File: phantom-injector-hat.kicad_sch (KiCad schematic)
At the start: 40 parts, among them J1 Conn_02x20_Odd_Even, J2 Conn_02x03_Top_Bottom, J3 Conn_01x03, J4 Conn_01x03, SW1 SW_SPST, U1 LT8362EMSE-PBF

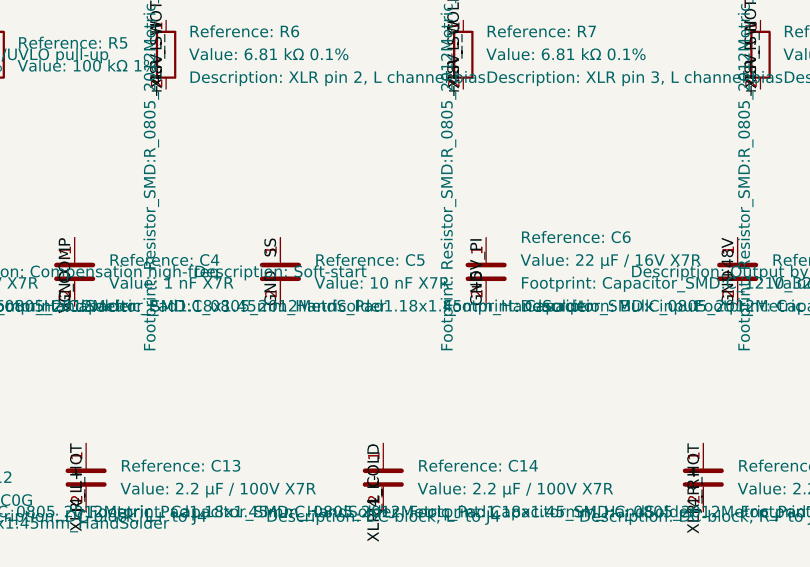
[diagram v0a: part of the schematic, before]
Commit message: Raise C5 soft-start cap from 10nF to 22nF; resolve item #7
Analytical Pi 5V inrush check (DESIGN_DOC §6 item 7) found the
original 10 nF gives a calculated ~750 mA input draw for 8 ms
during soft-start — over the 600 mA HAT continuous spec.

Bumping C5 to 22 nF lengthens t_ss from ~8 ms to ~17.6 ms,
cutting peak input current to ~342 mA (comfortably under HAT
budget). Steady-state input draw post-startup is ~34 mA at
full phantom load. Tradeoff is a 10 ms slower startup —
irrelevant for phantom power.

Schematic, BOM, DigiKey order CSV, and DESIGN_DOC all updated.
Sourced as Kemet 399-17886-1-ND after Yageo CC0805 Mfr PN
mis-resolved on DigiKey order pad.

Co-Authored-By: Claude Opus 4.7 <noreply@anthropic.com>
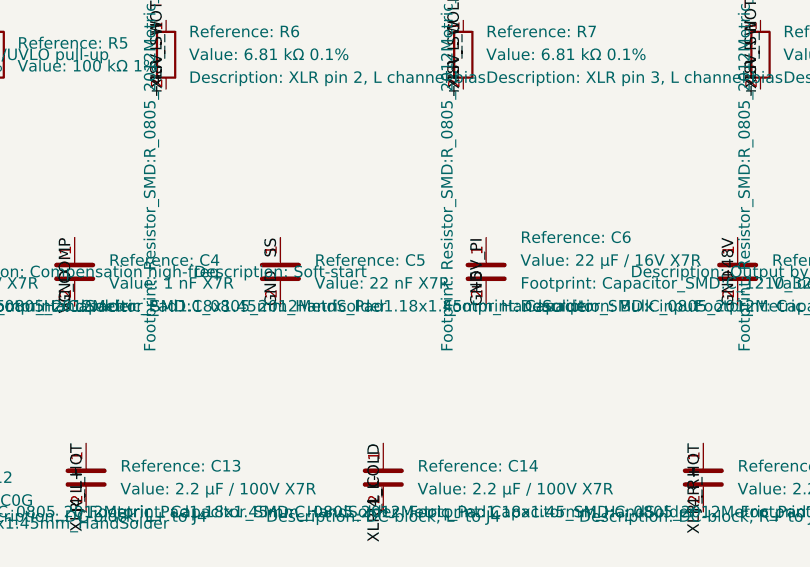
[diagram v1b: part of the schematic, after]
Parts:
- C5: value 10 nF X7R -> 22 nF X7R

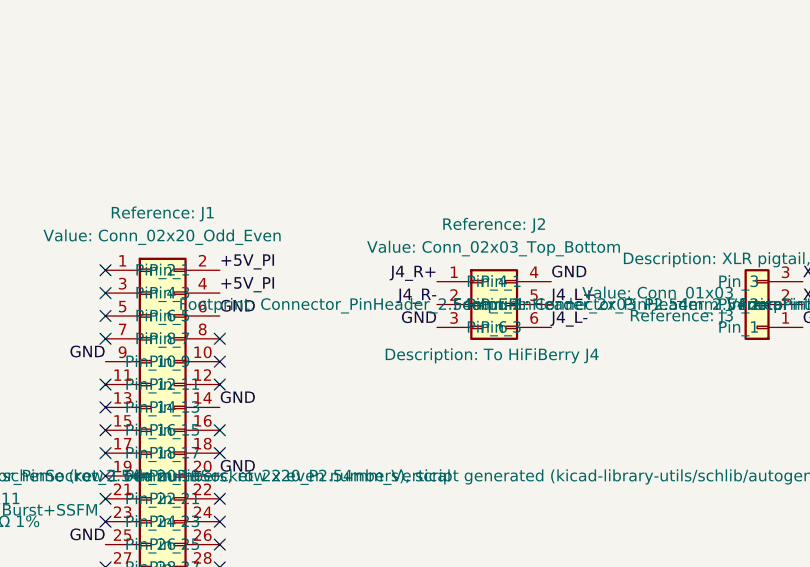
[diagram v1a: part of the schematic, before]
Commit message: Fix J2 right channel R+/R- swap; resolve item #5
Re-verified §3.4 HiFiBerry J4 pinout against the DAC2 ADC Pro
datasheet (hifiberry.com/docs/data-sheets/datasheet-dac2-adc-pro/).
Found a bug: §3.4 had J2 pin 1 = R+, pin 2 = R-, but the datasheet
specifies pin 1 = in R-, pin 2 = in R+ (pin 1 = left bottom corner).
Without the fix the right channel polarity would be inverted vs
the left, breaking stereo imaging and partially cancelling any
downstream mono sum.

- wire_schematic.py NETLIST: J2 pin 1/2 net assignments swapped
- phantom-injector-hat.kicad_sch: regenerated labels via
  wire_schematic.py (large diff is noise from fresh label UUIDs;
  functional change is only J2 pins 1 and 2)
- DESIGN_DOC.md §3.4 pinout table corrected
- DESIGN_DOC.md §6 item 5 marked resolved

After pulling: run Tools > Update PCB from Schematic (F8) in
KiCad PCB editor to propagate the netname swap.

Co-Authored-By: Claude Opus 4.7 <noreply@anthropic.com>
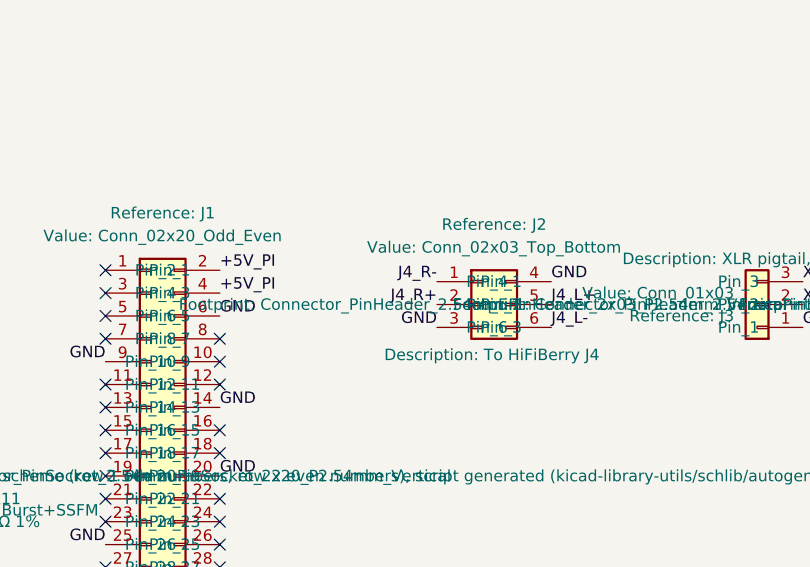
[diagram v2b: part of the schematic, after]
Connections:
- net J4_R+: now also J2.2 (Pin_2); no longer J2.1 (Pin_1)
- net J4_R-: now also J2.1 (Pin_1); no longer J2.2 (Pin_2)
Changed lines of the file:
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@@
+		)
+	)
+	(label "J4_R-"
+		(at 176.53 160.02 180)
+		(effects
+			(font
+				(size 1.27 1.27)
+			)
+			(justify right bottom)
 		)
 	)
 	(label "J4_R+"
-		(at 176.53 160.02 180)
-		(effects
-			(font
-				(size 1.27 1.27)
-			)
-			(justify right bottom)
-		)
-	)
-	(label "J4_R-"
 		(at 176.53 162.56 180)
 		(effects
@@
 	)
 	(label "GND"
+		(at 139.7 168.91 180)
+		(effects
+			(font
+				(size 1.27 1.27)
+			)
+			(justify right bottom)
+		)
+	)
+	(label "GND"
 		(at 152.4 181.61 0)
 		(effects
@@
 	)
 	(label "GND"
+		(at 139.7 207.01 180)
+		(effects
+			(font
+				(size 1.27 1.27)
+			)
+			(justify right bottom)
+		)
+	)
+	(label "GND"
 		(at 139.7 189.23 180)
 		(effects
@@
 	)
 	(label "GND"
+		(at 152.4 199.39 0)
+		(effects
+			(font
+				(size 1.27 1.27)
+			)
+			(justify left bottom)
+		)
+	)
+	(label "GND"
 		(at 152.4 173.99 0)
 		(effects
@@
 	)
 	(label "GND"
-		(at 152.4 199.39 0)
-		(effects
-			(font
-				(size 1.27 1.27)
-			)
-			(justify left bottom)
-		)
-	)
-	(label "GND"
 		(at 152.4 194.31 0)
 		(effects
@@
 		)
 	)
-	(label "GND"
-		(at 139.7 168.91 180)
-		(effects
-			(font
-				(size 1.27 1.27)
-			)
-			(justify right bottom)
-		)
-	)
-	(label "GND"
-		(at 139.7 207.01 180)
-		(effects
-			(font
-				(size 1.27 1.27)
-			)
-			(justify right bottom)
+	(label "+5V_PI"
+		(at 152.4 158.75 0)
+		(effects
+			(font
+				(size 1.27 1.27)
+			)
+			(justify left bottom)
 		)
 	)
@@
 		)
 	)
-	(label "+5V_PI"
-		(at 152.4 158.75 0)
-		(effects
-			(font
-				(size 1.27 1.27)
-			)
-			(justify left bottom)
-		)
-	)
 	(no_connect (at 45.72 185.42))
-	(no_connect (at 139.7 171.45))
 	(no_connect (at 139.7 158.75))
-	(no_connect (at 139.7 191.77))
-	(no_connect (at 139.7 163.83))
-	(no_connect (at 139.7 194.31))
-	(no_connect (at 139.7 201.93))
-	(no_connect (at 152.4 176.53))
+	(no_connect (at 139.7 173.99))
+	(no_connect (at 152.4 184.15))
+	(no_connect (at 139.7 199.39))
+	(no_connect (at 152.4 179.07))
+	(no_connect (at 152.4 168.91))
+	(no_connect (at 139.7 196.85))
 	(no_connect (at 139.7 179.07))
 	(no_connect (at 152.4 201.93))
+	(no_connect (at 152.4 166.37))
+	(no_connect (at 139.7 163.83))
+	(no_connect (at 152.4 189.23))
 	(no_connect (at 152.4 204.47))
-	(no_connect (at 152.4 184.15))
+	(no_connect (at 152.4 186.69))
+	(no_connect (at 152.4 171.45))
+	(no_connect (at 139.7 161.29))
+	(no_connect (at 139.7 194.31))
+	(no_connect (at 152.4 176.53))
+	(no_connect (at 152.4 191.77))
+	(no_connect (at 139.7 181.61))
+	(no_connect (at 139.7 184.15))
+	(no_connect (at 152.4 196.85))
 	(no_connect (at 139.7 204.47))
-	(no_connect (at 139.7 161.29))
-	(no_connect (at 139.7 173.99))
-	(no_connect (at 139.7 184.15))
+	(no_connect (at 139.7 201.93))
+	(no_connect (at 139.7 171.45))
+	(no_connect (at 139.7 176.53))
+	(no_connect (at 139.7 186.69))
+	(no_connect (at 139.7 191.77))
+	(no_connect (at 152.4 207.01))
 	(no_connect (at 139.7 166.37))
-	(no_connect (at 152.4 189.23))
-	(no_connect (at 152.4 179.07))
-	(no_connect (at 152.4 196.85))
-	(no_connect (at 152.4 191.77))
-	(no_connect (at 139.7 199.39))
-	(no_connect (at 152.4 166.37))
-	(no_connect (at 152.4 171.45))
-	(no_connect (at 139.7 196.85))
-	(no_connect (at 139.7 176.53))
-	(no_connect (at 152.4 168.91))
-	(no_connect (at 152.4 186.69))
-	(no_connect (at 152.4 207.01))
-	(no_connect (at 139.7 181.61))
-	(no_connect (at 139.7 186.69))
 )

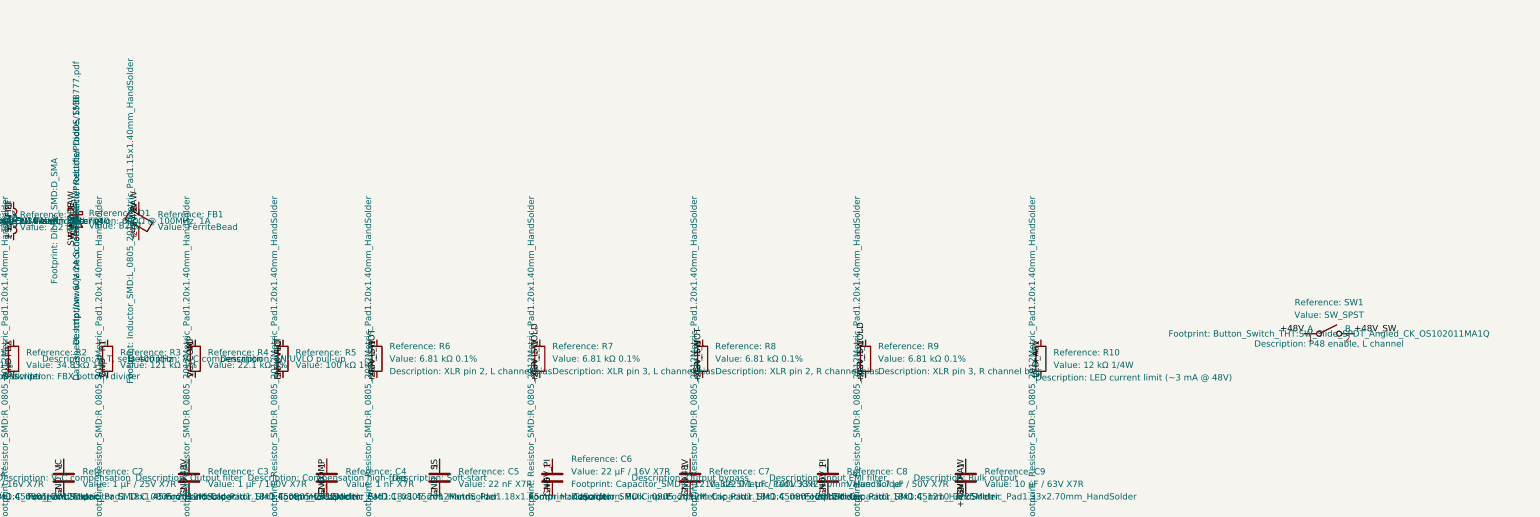
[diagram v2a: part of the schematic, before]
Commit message: LED follows switch; SW1 active mute via SPDT pin3→GND; FB1 footprint fix
LED indicator (D2/R10): moved R10 pin 1 from +48V (always-on
boost output) to +48V_SW (switched). The LED now indicates
"phantom is enabled" rather than "boost converter is running"
— standard pro-audio convention.

SW1 upgraded SPST → SPDT to actively drain the phantom rail
on mute. Pin 2 (common) = +48V_SW output to R6-R9; pin 1
(throw A) = +48V; pin 3 (throw B) = GND. Flipping the switch
off now actively pulls +48V_SW to GND through R6-R9, giving
a cleaner mute than letting the rail decay across the DC-block
caps. Schematic symbol was swapped from Switch:SW_SPST to
Switch:SW_SPDT in eeschema; wire_schematic.py LIB_PINS gained
SW_SPDT pin coords; NETLIST gained SW1 pin 3 = GND.

FB1 footprint corrected: schematic had typo
'L_0805_2012Metric_Pad1.15x1.40mm_HandSolder' (which does
not exist in KiCad's library) — fixed to the canonical
'L_0805_2012Metric_Pad1.05x1.20mm_HandSolder' that BOM.csv
already references. This was blocking F8 sync to PCB.

DESIGN_DOC §3.1 net members table updated to reflect R10 on
+48V_SW, SW1 pin 3 on GND. D2 BOM description updated from
'+48V rail indicator' to 'Phantom enable indicator'.

PCB synced via Update PCB from Schematic (F8) in PCB editor.

Co-Authored-By: Claude Opus 4.7 <noreply@anthropic.com>
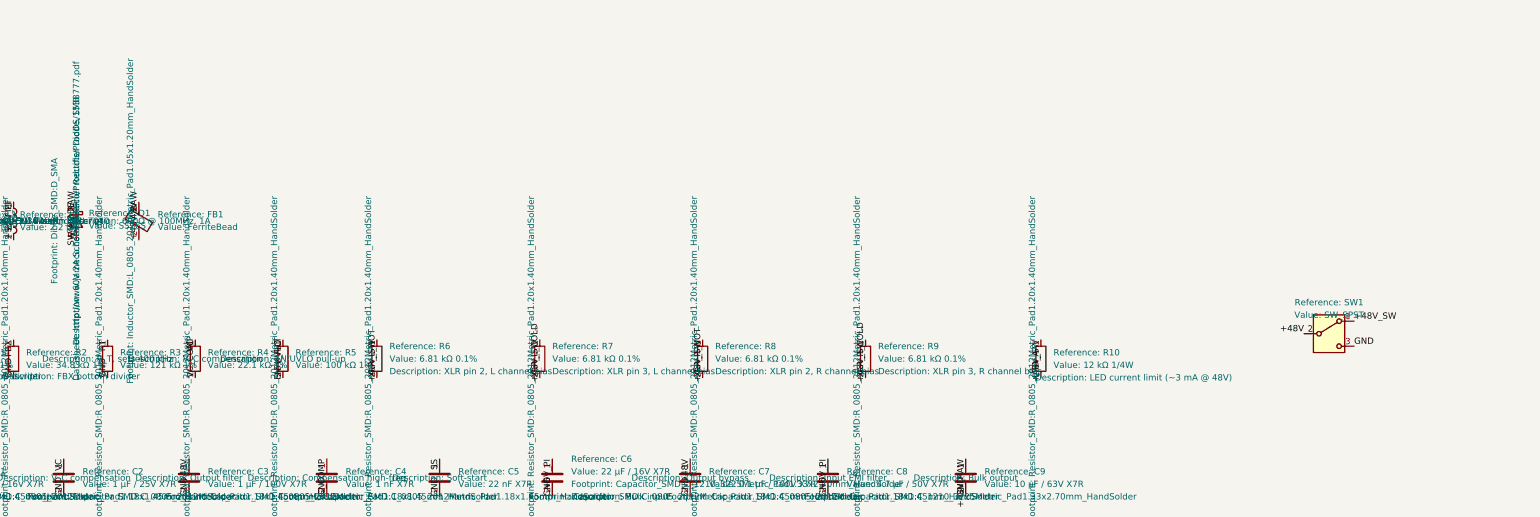
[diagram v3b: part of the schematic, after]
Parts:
- D1: value B260 -> SS26S
- FB1: footprint Inductor_SMD:L_0805_2012Metric_Pad1.15x1.40mm_HandSolder -> Inductor_SMD:L_0805_2012Metric_Pad1.05x1.20mm_HandSolder
- SW1: symbol Switch:SW_SPST -> Switch:SW_SPDT
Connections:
- net +48V: now also SW1.2 (B); no longer R10.1, SW1.1 (A)
- net +48V_SW: now also R10.1, SW1.1 (A); no longer SW1.2 (B)
- net GND: now also SW1.3 (C)

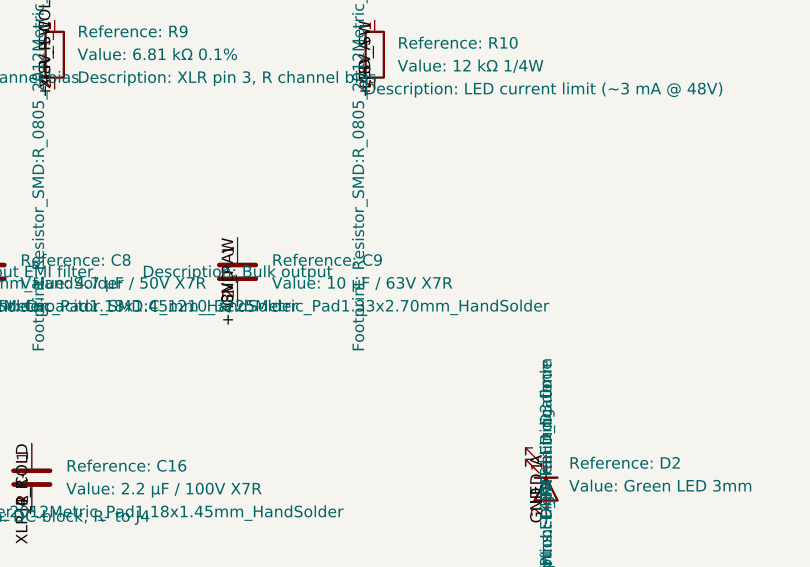
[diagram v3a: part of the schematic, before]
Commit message: C9: switch from Yageo 63V to TDK 100V (1210); fix package mis-order
Original order had Yageo 311-1577-2-ND for C9, which silently
resolved on DigiKey to a 0201 part instead of the intended 1210.
Re-ordered as TDK C3225X7R2A106K250AC (10µF / 100V / X7R /
1210). Bumping voltage spec 63V → 100V at the same time for
better derating headroom on the 48V rail — the 0805 vs 1210
package was already locked in by board geometry.

- digikey-order-5units.csv: C9 line updated to TDK Mfr PN
- BOM.csv: C9 row rewritten with new mfr/PN/voltage; stale
  50V→63V upgrade note replaced with the sourcing story
- BOM.csv: OPEN ITEMS #11 added with mis-resolution closeout
- DESIGN_DOC.md §2.1 table + rationale paragraph updated
- phantom-injector-hat.kicad_sch: C9 value text → 100V
- phantom-injector-hat.kicad_pcb: route UUID churn from a
  prior F8 sync, bundled in

No PCB footprint change — both old and new caps are 1210.

Co-Authored-By: Claude Opus 4.7 <noreply@anthropic.com>
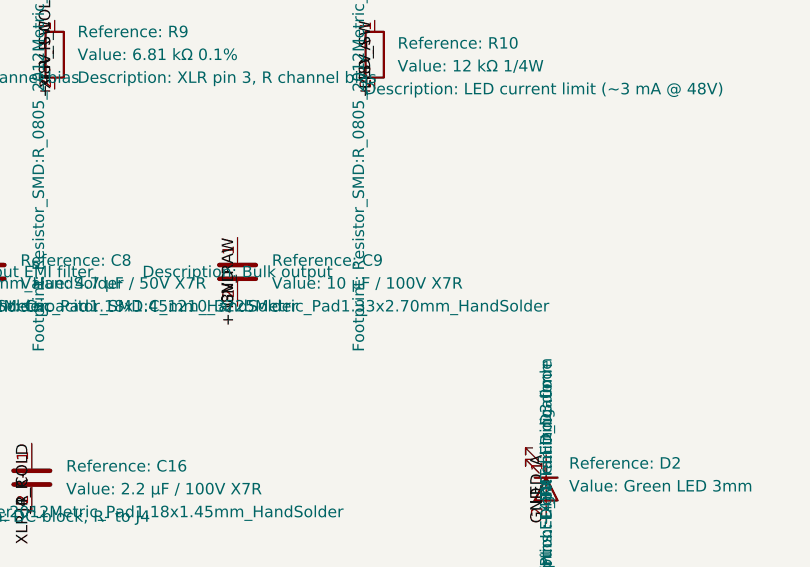
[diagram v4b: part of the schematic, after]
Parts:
- C9: value 10 µF / 63V X7R -> 10 µF / 100V X7R
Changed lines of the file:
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@@
 			)
 		)
-		(property "Value" "10 µF / 63V X7R"
+		(property "Value" "10 µF / 100V X7R"
 			(at 250.19 83.8199 0)
 			(show_name yes)

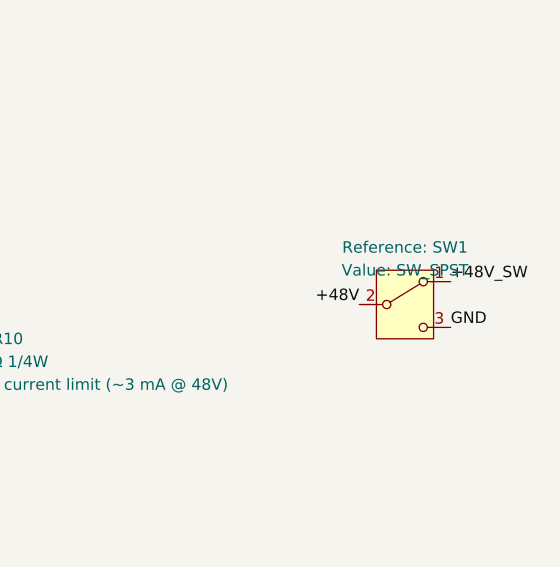
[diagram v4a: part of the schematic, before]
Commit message: Fix SW1 OFF throw shorting +48V to GND; sync C9 value
The schematic had drifted from wire_schematic.py: SW1's common (pin 2,
middle pad) sat on +48V with pin 3 on GND, so switching phantom off
shorted the boost output. Re-ran wire_schematic.py (netlist diff is SW1
only), swapped SW1 pad 1/2 nets on the PCB, and rerouted: +48V now drops
from C3 through a via and a short B.Cu link to pad 1; +48V_SW passes over
pad 1 into pad 2 on F.Cu.

Also sync the C9 footprint value to the schematic (100V), which clears
the only schematic-parity finding. DRC unchanged (1 documented exception,
0 unconnected), ERC 0 errors. Golden netlist re-saved; renders refreshed.

Co-Authored-By: Claude Opus 5.5 <noreply@anthropic.com>
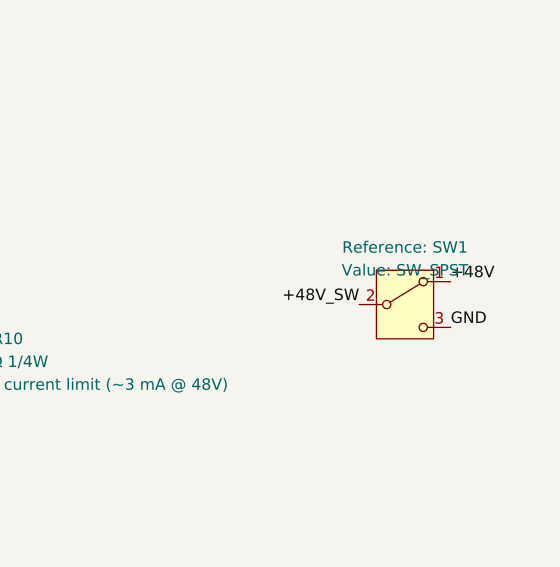
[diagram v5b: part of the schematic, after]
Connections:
- net +48V: now also SW1.1 (A); no longer SW1.2 (B)
- net +48V_SW: now also SW1.2 (B); no longer SW1.1 (A)
